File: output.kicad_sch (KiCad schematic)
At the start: 26 parts, among them U32 74HCT107, U33 74LS139, U35 LTC-5723HR, U37 AT28C64B, U4 LMC555xN, U8 74HCT173, U9 74HCT173

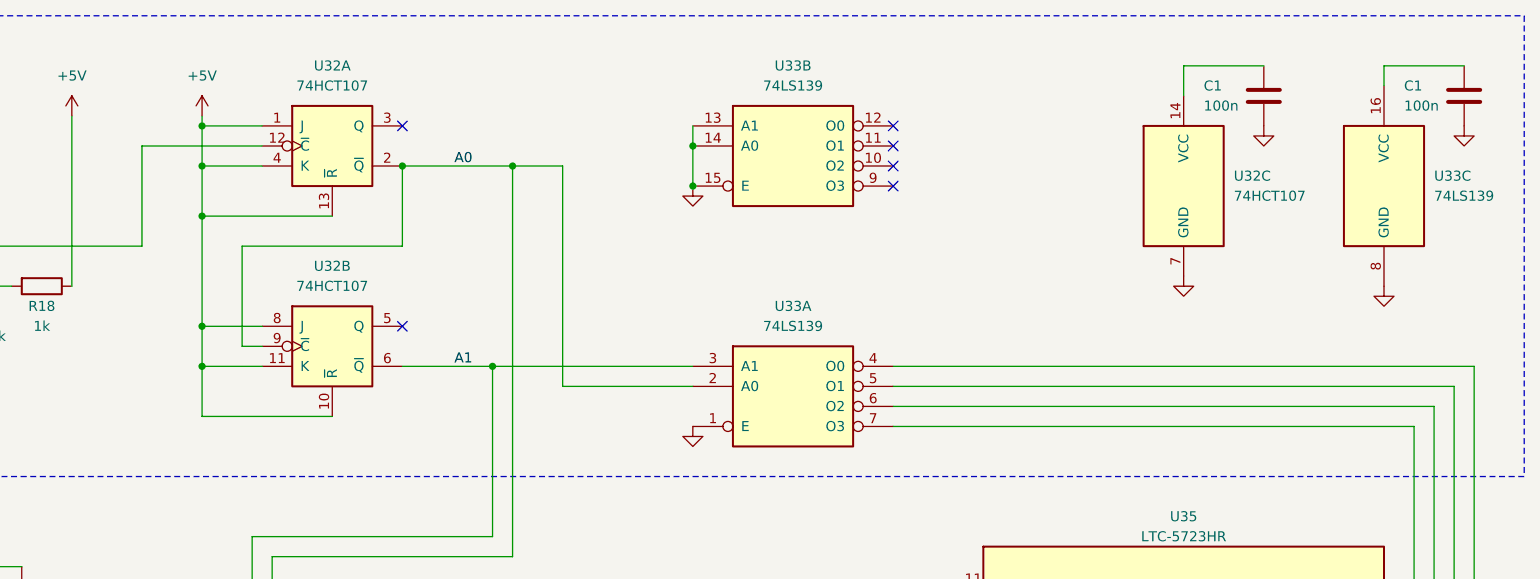
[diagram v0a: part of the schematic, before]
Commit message: changed symbols
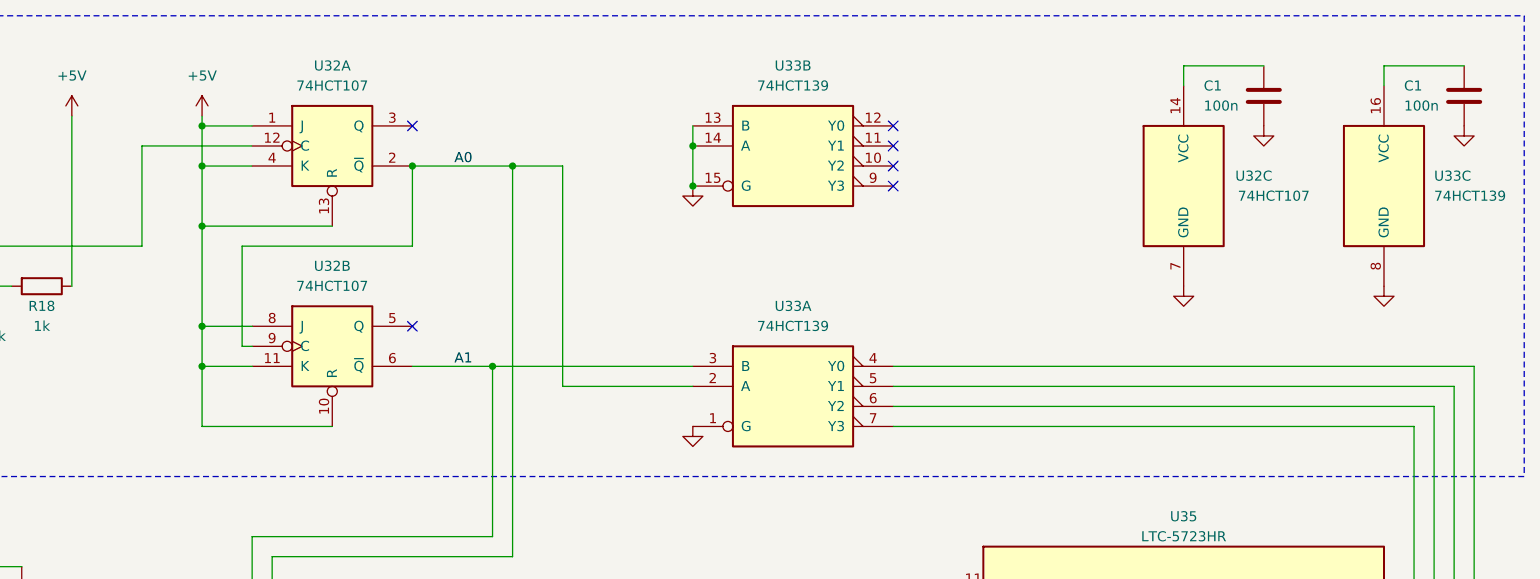
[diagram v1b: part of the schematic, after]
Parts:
- U33: value 74LS139 -> 74HCT139; symbol 74xx:74LS139 -> 01_my_library:74HCT139

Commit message: some cleanup
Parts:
- renumbered R99 to R100, R100 to R101, R101 to R102, R102 to R103, R103 to R104, R104 to R105, R105 to R106, R106 to R107, R98 to R99

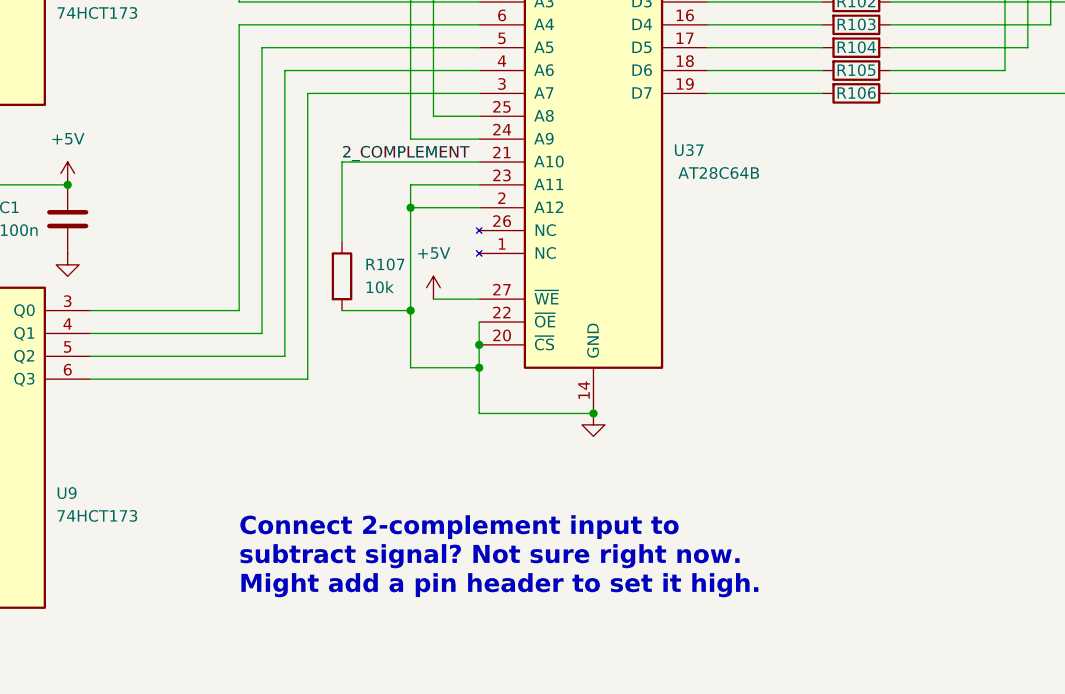
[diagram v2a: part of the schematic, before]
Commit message: add arduino headers for programming
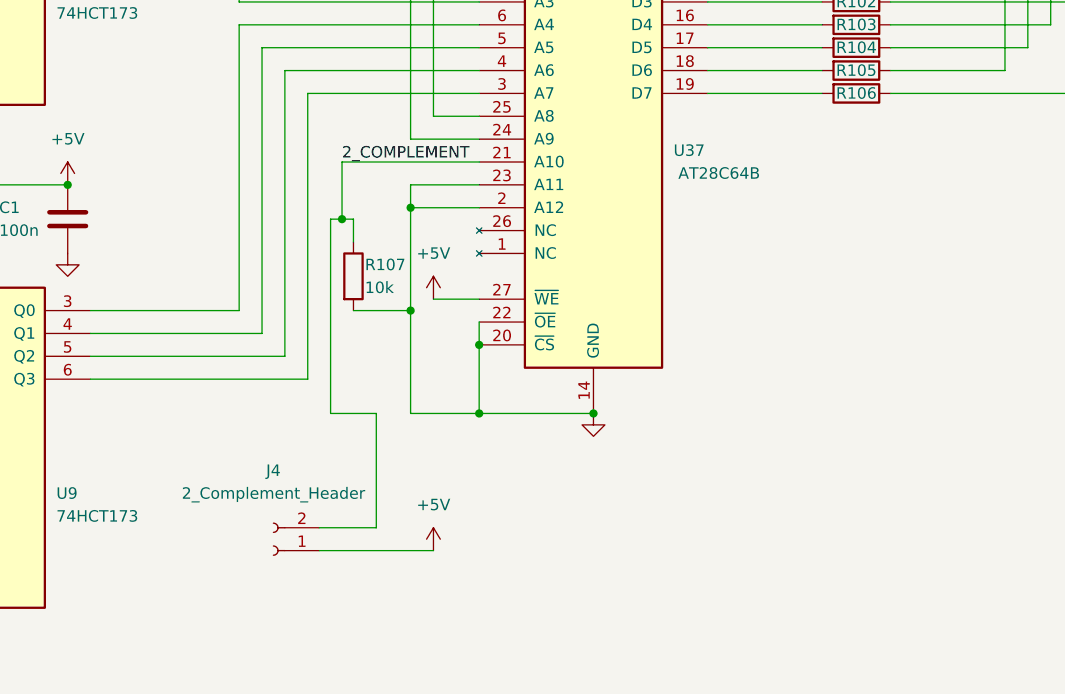
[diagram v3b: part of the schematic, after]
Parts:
- added J4: 2_Complement_Header, Connector_PinSocket_2.54mm:PinSocket_1x02_P2.54mm_Vertical, symbol Connector:Conn_01x02_Socket
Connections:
- net +5V: now also J4.1 (Pin_1)
- net 2_COMPLEMENT: now also J4.2 (Pin_2)
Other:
- note removed: "Connect 2-complement input to subtract signal? Not sure right now. Might add a pin header to set it high."
- moved on the sheet: R107
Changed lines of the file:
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@@
   (junction (at 119.38 140.97) (diameter 0) (color 0 0 0 0)
   )
+  (junction (at 127 163.83) (diameter 0) (color 0 0 0 0)
+  )
   (junction (at 139.7 163.83) (diameter 0) (color 0 0 0 0)
   )
@@
   (junction (at 139.7 96.52) (diameter 0) (color 0 0 0 0)
   )
-  (junction (at 127 158.75) (diameter 0) (color 0 0 0 0)
-  )
   (junction (at 33.02 127) (diameter 0) (color 255 0 0 1)
+  )
+  (junction (at 111.76 142.24) (diameter 0) (color 0 0 0 0)
   )
   (junction (at 149.86 58.42) (diameter 0) (color 0 0 0 0)
@@
     (stroke (width 0) (type default))
   )
+  (wire (pts (xy 115.57 163.83) (xy 110.49 163.83))
+    (stroke (width 0) (type default))
+  )
   (wire (pts (xy 54.61 111.76) (xy 58.42 111.76))
     (stroke (width 0) (type default))
@@
     (stroke (width 0) (type default))
   )
-  (wire (pts (xy 111.76 152.4) (xy 119.38 152.4))
+  (wire (pts (xy 113.03 152.4) (xy 119.38 152.4))
     (stroke (width 0) (type default))
   )
@@
     (stroke (width 0) (type default))
   )
+  (wire (pts (xy 109.22 176.53) (xy 115.57 176.53))
+    (stroke (width 0) (type default))
+  )
   (wire (pts (xy 152.4 120.65) (xy 165.1 120.65))
+    (stroke (width 0) (type default))
+  )
+  (wire (pts (xy 113.03 142.24) (xy 111.76 142.24))
     (stroke (width 0) (type default))
   )
@@
     (stroke (width 0) (type default))
   )
+  (wire (pts (xy 110.49 142.24) (xy 111.76 142.24))
+    (stroke (width 0) (type default))
+  )
   (wire (pts (xy 54.61 165.1) (xy 58.42 165.1))
     (stroke (width 0) (type default))
@@
     (stroke (width 0) (type default))
   )
-  (wire (pts (xy 119.38 158.75) (xy 127 158.75))
+  (wire (pts (xy 119.38 163.83) (xy 127 163.83))
     (stroke (width 0) (type default))
   )
@@
     (stroke (width 0) (type default))
   )
-  (wire (pts (xy 111.76 135.89) (xy 111.76 144.78))
+  (wire (pts (xy 111.76 135.89) (xy 111.76 142.24))
     (stroke (width 0) (type default))
   )
@@
     (stroke (width 0) (type default))
   )
-  (wire (pts (xy 127 158.75) (xy 127 163.83))
+  (wire (pts (xy 127 156.21) (xy 127 163.83))
     (stroke (width 0) (type default))
   )
@@
   )
   (wire (pts (xy 113.03 27.94) (xy 119.38 27.94))
+    (stroke (width 0) (type default))
+  )
+  (wire (pts (xy 113.03 142.24) (xy 113.03 144.78))
     (stroke (width 0) (type default))
   )
@@
     (stroke (width 0) (type default))
   )
+  (wire (pts (xy 110.49 163.83) (xy 110.49 142.24))
+    (stroke (width 0) (type default))
+  )
   (wire (pts (xy 269.24 63.5) (xy 269.24 99.06))
     (stroke (width 0) (type default))
@@
     (stroke (width 0) (type default))
   )
+  (wire (pts (xy 109.22 179.07) (xy 121.92 179.07))
+    (stroke (width 0) (type default))
+  )
   (wire (pts (xy 172.72 128.27) (xy 203.2 128.27))
     (stroke (width 0) (type default))
   )
   (wire (pts (xy 83.82 154.94) (xy 102.87 154.94))
-    (stroke (width 0) (type default))
-  )
-  (wire (pts (xy 127 156.21) (xy 127 158.75))
     (stroke (width 0) (type default))
   )
@@
     (stroke (width 0) (type default))
   )
-  (wire (pts (xy 119.38 152.4) (xy 119.38 158.75))
+  (wire (pts (xy 119.38 152.4) (xy 119.38 163.83))
     (stroke (width 0) (type default))
   )
   (wire (pts (xy 152.4 118.11) (xy 165.1 118.11))
+    (stroke (width 0) (type default))
+  )
+  (wire (pts (xy 115.57 176.53) (xy 115.57 163.83))
     (stroke (width 0) (type default))
   )
@@
   (text "Logic for mulitplexing the display" (at 50.8 17.78 0)
     (effects (font (size 1.27 1.27)) (justify right bottom))
-  )
-  (text "Connect 2-complement input to \nsubtract signal? Not sure right now.\nMight add a pin header to set it high."
-    (at 100.33 184.15 0)
-    (effects (font (size 2 2) (thickness 0.4) bold) (justify left bottom))
   )
   (label "2_COMPLEMENT" (at 111.76 135.89 0) (fields_autoplaced)
@@
     )
   )
-  (symbol (lib_id "Device:R") (at 111.76 148.59 0) (unit 1)
-    (in_bom yes) (on_board yes) (dnp no) (fields_autoplaced)
+  (symbol (lib_id "Device:R") (at 113.03 148.59 0) (unit 1)
+    (in_bom yes) (on_board yes) (dnp no)
     (property "Reference" "R107" (at 114.3 147.32 0)
       (effects (font (size 1.27 1.27)) (justify left))
@@
       (effects (font (size 1.27 1.27)) (justify left))
     )
-    (property "Footprint" "Resistor_THT:R_Axial_DIN0204_L3.6mm_D1.6mm_P7.62mm_Horizontal" (at 109.982 148.59 90)
-      (effects (font (size 1.27 1.27)) hide)
-    )
-    (property "Datasheet" "~" (at 111.76 148.59 0)
+    (property "Footprint" "Resistor_THT:R_Axial_DIN0204_L3.6mm_D1.6mm_P7.62mm_Horizontal" (at 111.252 148.59 90)
+      (effects (font (size 1.27 1.27)) hide)
+    )
+    (property "Datasheet" "~" (at 113.03 148.59 0)
       (effects (font (size 1.27 1.27)) hide)
     )
@@
     )
   )
+  (symbol (lib_id "Connector:Conn_01x02_Socket") (at 104.14 179.07 180) (unit 1)
+    (in_bom yes) (on_board yes) (dnp no)
+    (property "Reference" "J4" (at 104.14 170.18 0)
+      (effects (font (size 1.27 1.27)))
+    )
+    (property "Value" "2_Complement_Header" (at 104.14 172.72 0)
+      (effects (font (size 1.27 1.27)))
+    )
+    (property "Footprint" "Connector_PinSocket_2.54mm:PinSocket_1x02_P2.54mm_Vertical" (at 104.14 179.07 0)
+      (effects (font (size 1.27 1.27)) hide)
+    )
+    (property "Datasheet" "~" (at 104.14 179.07 0)
+      (effects (font (size 1.27 1.27)) hide)
+    )
+    (pin "2")
+    (pin "1")
+    (instances
+      (project "8-bit-cpu"
+        (path "/100bb8d1-c3d6-4e1f-87b6-72e4e187243c/2c3402b7-c2ba-43ce-9f44-0fa5e5dc9ef7"
+          (reference "J4") (unit 1)
+        )
+      )
+    )
+  )
   (symbol (lib_id "Device:C") (at 34.29 52.07 0) (unit 1)
     (in_bom yes) (on_board yes) (dnp no)
@@
         )
       )
+    )
+  )
+  (symbol (lib_id "power:+5V") (at 121.92 179.07 0) (unit 1)
+    (in_bom yes) (on_board yes) (dnp no)
+    (property "Reference" "#PWR07" (at 121.92 182.88 0)
+      (effects (font (size 1.27 1.27)) hide)
+    )
+    (property "Value" "+5V" (at 121.92 173.99 0)
+      (effects (font (size 1.27 1.27)))
+    )
+    (property "Footprint" "" (at 121.92 179.07 0)
+      (effects (font (size 1.27 1.27)) hide)
+    )
+    (property "Datasheet" "" (at 121.92 179.07 0)
+      (effects (font (size 1.27 1.27)) hide)
+    )
+    (pin "1")
+    (instances
+      (project "8-bit-cpu"
+        (path "/100bb8d1-c3d6-4e1f-87b6-72e4e187243c/45eb39c3-c748-461e-8330-08aae1247dee"
+          (reference "#PWR07") (unit 1)
+        )
+        (path "/100bb8d1-c3d6-4e1f-87b6-72e4e187243c/2c3402b7-c2ba-43ce-9f44-0fa5e5dc9ef7"
+          (reference "#PWR0253") (unit 1)
+        )
+      )

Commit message: cleanup
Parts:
- C5: symbol Device:C_Polarized -> Device:C

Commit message: cleanup
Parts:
- renumbered R101 to R100, R102 to R101, R103 to R102, R104 to R103, R105 to R104, R106 to R105, R107 to R106, R99 to R98, R100 to R99

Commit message: readme
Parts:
- added C13: 10n, 01_my_library:C_Disc_D4.0mm_W2.6mm_P2.50mm, symbol Device:C
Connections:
- net GND: now also C13.2
- net RESET: now also C13.1
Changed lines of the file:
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@@
   (junction (at 152.4 33.02) (diameter 0) (color 0 0 0 0)
+  )
+  (junction (at 38.1 182.88) (diameter 0) (color 255 0 0 1)
   )
   (junction (at 119.38 140.97) (diameter 0) (color 0 0 0 0)
@@
   (wire (pts (xy 29.21 106.68) (xy 52.07 106.68))
     (stroke (width 0) (type default) (color 0 0 255 1))
+  )
+  (wire (pts (xy 38.1 182.88) (xy 38.1 186.69))
+    (stroke (width 0) (type default) (color 255 0 0 1))
   )
   (wire (pts (xy 54.61 109.22) (xy 58.42 109.22))
@@
     )
   )
+  (symbol (lib_id "power:GND") (at 38.1 194.31 0) (unit 1)
+    (in_bom yes) (on_board yes) (dnp no) (fields_autoplaced)
+    (property "Reference" "#PWR03" (at 38.1 200.66 0)
+      (effects (font (size 1.27 1.27)) hide)
+    )
+    (property "Value" "GND" (at 38.1 199.39 0)
+      (effects (font (size 1.27 1.27)) hide)
+    )
+    (property "Footprint" "" (at 38.1 194.31 0)
+      (effects (font (size 1.27 1.27)) hide)
+    )
+    (property "Datasheet" "" (at 38.1 194.31 0)
+      (effects (font (size 1.27 1.27)) hide)
+    )
+    (pin "1")
+    (instances
+      (project "8-bit-cpu"
+        (path "/100bb8d1-c3d6-4e1f-87b6-72e4e187243c/45eb39c3-c748-461e-8330-08aae1247dee"
+          (reference "#PWR03") (unit 1)
+        )
+        (path "/100bb8d1-c3d6-4e1f-87b6-72e4e187243c/651dfbaf-e340-4976-8216-793c5a5aaa3b"
+          (reference "#PWR038") (unit 1)
+        )
+        (path "/100bb8d1-c3d6-4e1f-87b6-72e4e187243c/3568514a-e420-48fa-9fd5-7a290120765b"
+          (reference "#PWR056") (unit 1)
+        )
+        (path "/100bb8d1-c3d6-4e1f-87b6-72e4e187243c/2c3402b7-c2ba-43ce-9f44-0fa5e5dc9ef7"
+          (reference "#PWR0266") (unit 1)
+        )
+      )
+    )
+  )
   (symbol (lib_id "Device:R") (at 168.91 128.27 270) (unit 1)
     (in_bom yes) (on_board yes) (dnp no)
@@
         )
       )
+    )
+  )
+  (symbol (lib_id "Device:C") (at 38.1 190.5 0) (unit 1)
+    (in_bom yes) (on_board yes) (dnp yes) (fields_autoplaced)
+    (property "Reference" "C13" (at 41.91 189.23 0)
+      (effects (font (size 1.27 1.27)) (justify left))
+    )
+    (property "Value" "10n" (at 41.91 191.77 0)
+      (effects (font (size 1.27 1.27)) (justify left))
+    )
+    (property "Footprint" "01_my_library:C_Disc_D4.0mm_W2.6mm_P2.50mm" (at 39.0652 194.31 0)
+      (effects (font (size 1.27 1.27)) hide)
+    )
+    (property "Datasheet" "~" (at 38.1 190.5 0)
+      (effects (font (size 1.27 1.27)) hide)
+    )
+    (pin "1")
+    (pin "2")
+    (instances
+      (project "8-bit-cpu"
+        (path "/100bb8d1-c3d6-4e1f-87b6-72e4e187243c/651dfbaf-e340-4976-8216-793c5a5aaa3b"
+          (reference "C13") (unit 1)
+        )
+        (path "/100bb8d1-c3d6-4e1f-87b6-72e4e187243c/2c3402b7-c2ba-43ce-9f44-0fa5e5dc9ef7"
+          (reference "C78") (unit 1)
+        )
+      )
